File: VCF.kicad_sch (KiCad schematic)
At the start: 79 parts, among them K10 SW_SPST, K7 SW_SPST, K8 SW_SPST, K9 SW_SPST, P10 100k, P11 100k, P12 100k, P14 100k, P16 22k, P8 50k, P9 50k, Q20 BF244A, Q21 BC214, Q22 BC214, Q23 BF244A, Q24 BC214, Q25 BC214, Q26 BC182B, U10 UA747, U12 CA3080A, U13 CA3080A, U8 UA747, U9 CA3080A

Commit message: Fix PCB errors
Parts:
- added C_Sin1 (x20): Conn_01x01, Connector_PinHeader_2.54mm:PinHeader_1x01_P2.54mm_Vertical, symbol Connector_Generic:Conn_01x01
- C25: footprint Capacitor_THT:CP_Radial_D6.3mm_P2.50mm -> Capacitor_THT:CP_Radial_D8.0mm_P5.00mm
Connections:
- net CV: now also C_Sin1.1 (Pin_1)
- net ENVELOPE: now also C_Sin1.1 (Pin_1)
- net LFO_OUT: now also C_Sin1.1 (Pin_1)
- net at C19.1, K10.2 (B), R91.1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: now also C_Sin1.1 (Pin_1)
- net at P14.1, Q24.1 (B), R116.2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: now also C_Sin1.1 (Pin_1)
- net at C18.2, P11.2, R98.1: now also C_Sin1.1 (Pin_1)
- net at P8.2, R95.1: now also C_Sin1.1 (Pin_1)
- net at P9.2, R96.1: now also C_Sin1.1 (Pin_1)
- net at P10.2, R97.1: now also C_Sin1.1 (Pin_1)
- net at K7.1 (A), R94.1: now also C_Sin1.1 (Pin_1)
- net at C22.1, K8.2 (B), Q23.3 (S)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: now also C_Sin1.1 (Pin_1)
- net at K9.2 (B), P12.1, Q20.3 (S)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: now also C_Sin1.1 (Pin_1), C_Sin1.1 (Pin_1)
- net at P14.2, R114.2: now also C_Sin1.1 (Pin_1)
- net at P16.3, R136.1: now also C_Sin1.1 (Pin_1)
- net at P12.2, R104.1: now also C_Sin1.1 (Pin_1)
- net at P12.3, R106.2: now also C_Sin1.1 (Pin_1)
- net at K8.1 (A), R123.2: now also C_Sin1.1 (Pin_1)
- net at K10.1 (A), R121.2: now also C_Sin1.1 (Pin_1)
- net at K9.1 (A), R122.2: now also C_Sin1.1 (Pin_1)
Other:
- note removed: "15V? Or GND?"
- moved on the sheet: C22, K10, K7, K8, K9, P10, P11, P8, P9, R104, R106, R108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

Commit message: Kicad update
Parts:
- renumbered C_Sin1 to K10-1, C_Sin1 to K10-2, C_Sin1 to K7-1, C_Sin1 to K7-2, C_Sin1 to K8-1, C_Sin1 to K8-2, C_Sin1 to K9-1, C_Sin1 to K9-2, C_Sin1 to P10-3, C_Sin1 to P11-3, C_Sin1 to P12-1, C_Sin1 to P12-2, C_Sin1 to P12-3, C_Sin1 to P13-1, C_Sin1 to P14-1, C_Sin1 to P14-3, C_Sin1 to P8-1, C_Sin1 to P8-3, C_Sin1 to P9-1, C_Sin1 to P9-3

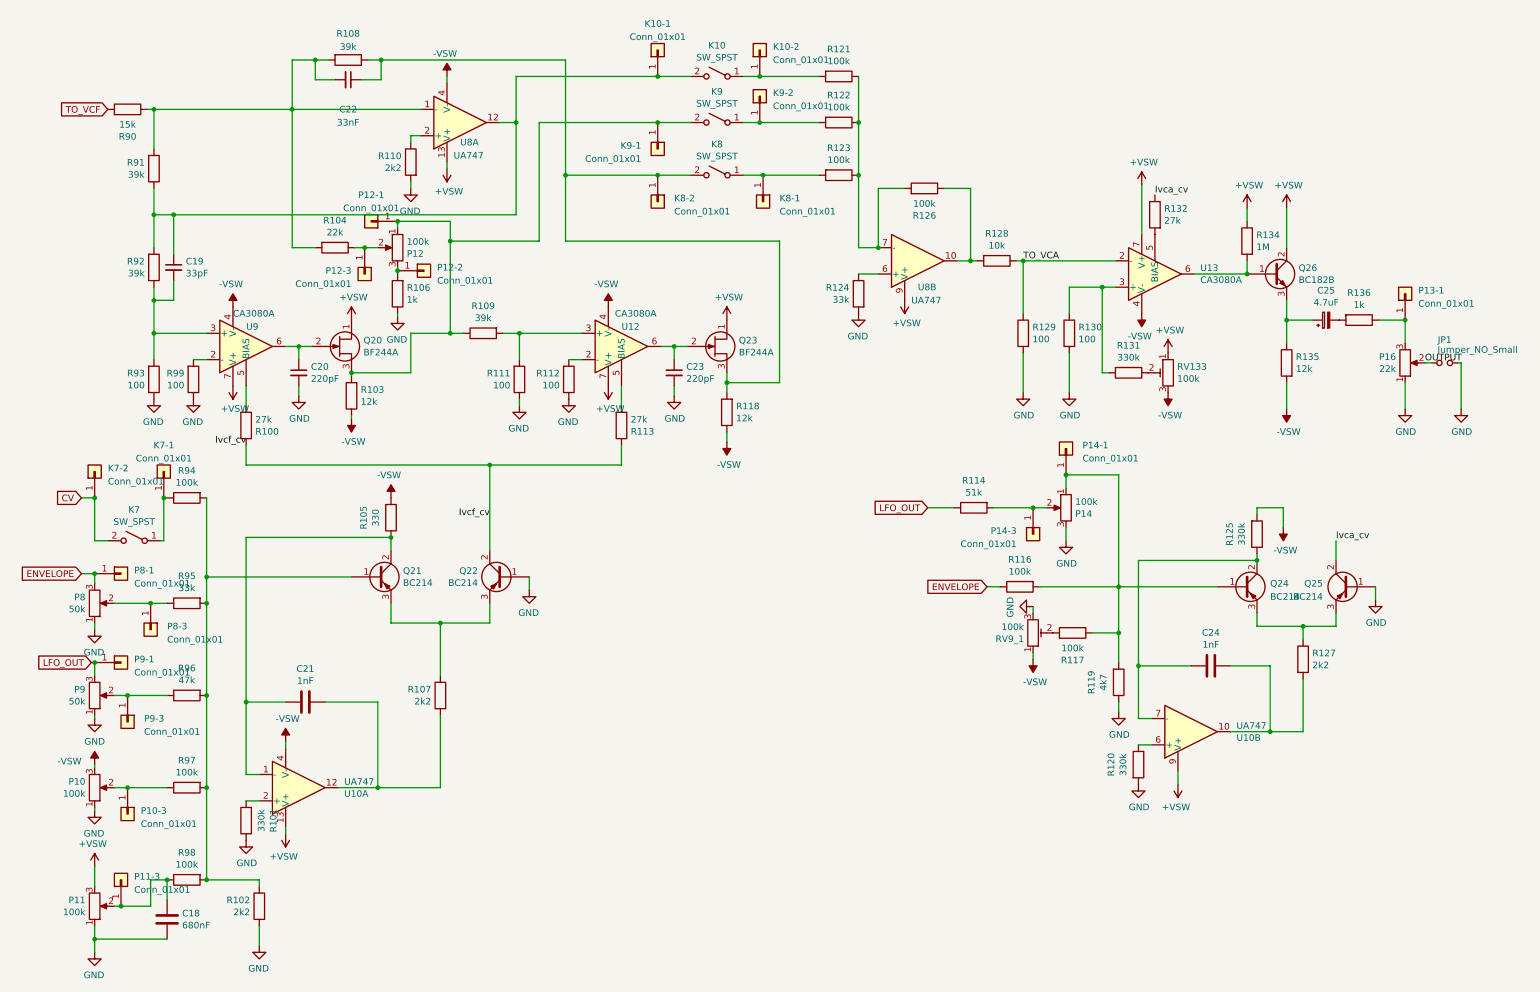
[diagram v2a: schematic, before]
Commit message: Replace symbols with new library
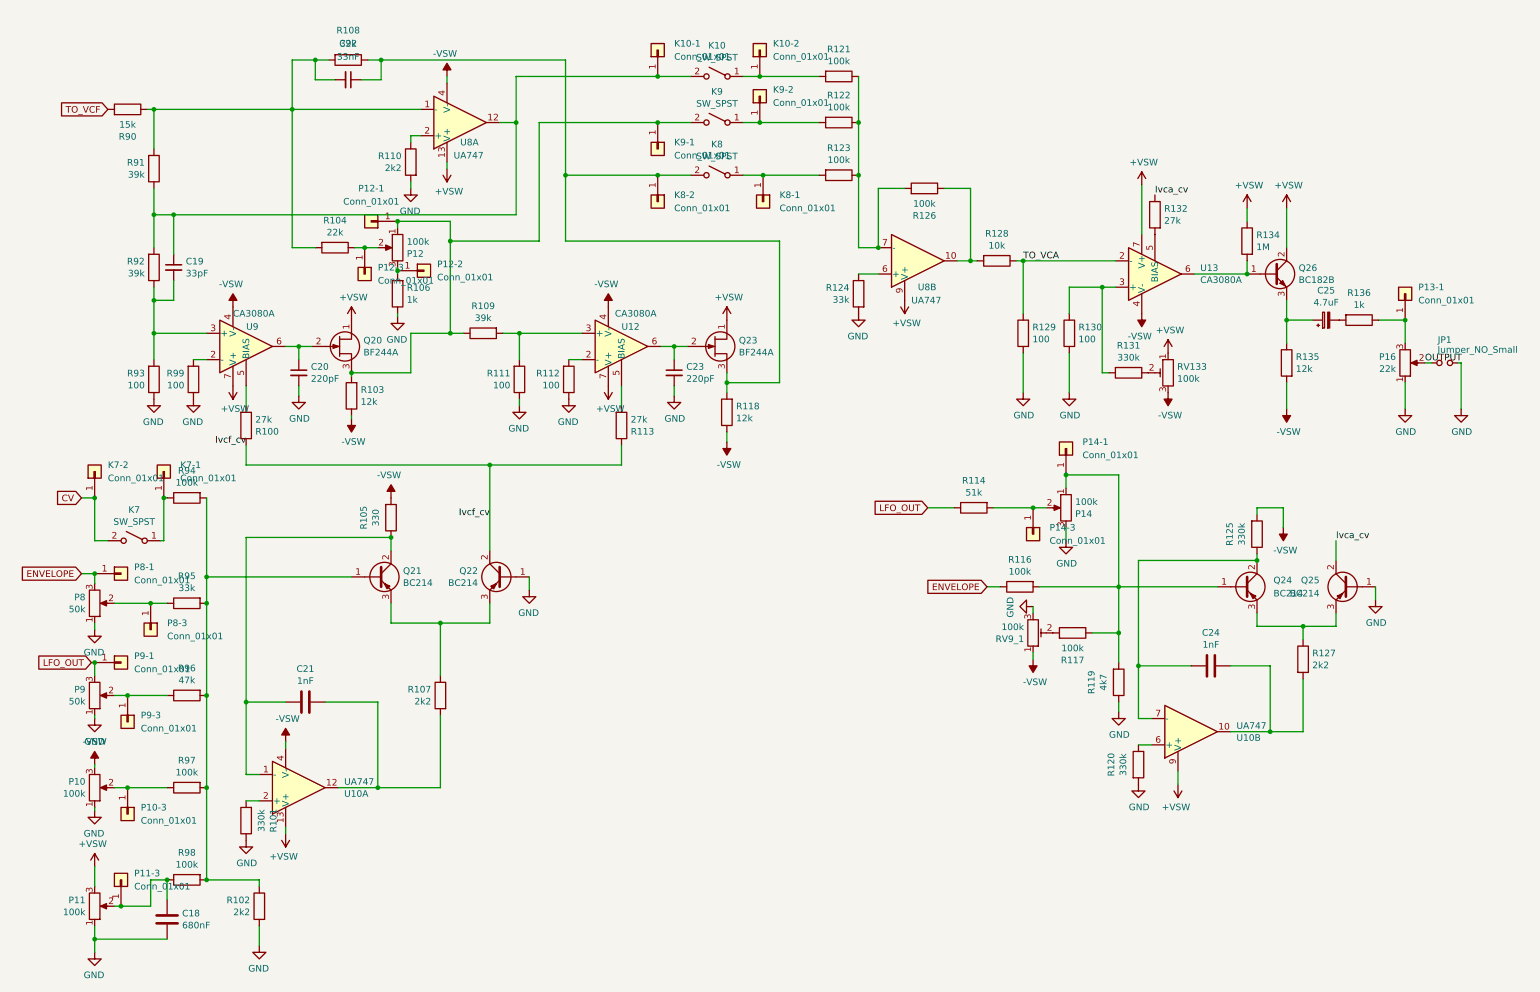
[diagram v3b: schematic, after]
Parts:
- C18, C19, C20, C21, C22, C23, C24: footprint Capacitor_THT:C_Disc_D5.0mm_W2.5mm_P5.00mm -> (none)
- C25: footprint Capacitor_THT:CP_Radial_D8.0mm_P5.00mm -> (none)
- JP1: footprint Connector_PinHeader_2.54mm:PinHeader_1x02_P2.54mm_Vertical -> (none)
- K10, K7, K8, K9, P10, P11, P12, P14, P16, P8, P9: footprint Connector_PinSocket_2.54mm:PinSocket_1x03_P2.54mm_Vertical -> (none)
- K10-1, K10-2, K7-1, K7-2, K8-1, K8-2, K9-1, K9-2, P10-3, P11-3, P12-1, P12-2, P12-3, P13-1, P14-1, P14-3, P8-1, P8-3, P9-1, P9-3: footprint Connector_PinHeader_2.54mm:PinHeader_1x01_P2.54mm_Vertical -> (none)
- Q20, Q23: footprint Package_TO_SOT_THT:TO-92L_Inline_Wide -> Package_TO_SOT_THT:TO-92_Inline
- Q21, Q22, Q24, Q25: symbol Device:Q_PNP_BCE -> Transistor_BJT:Q_PNP_BCE
- Q26: symbol Device:Q_NPN_BCE -> Transistor_BJT:Q_NPN_BCE
- R100, R101, R102, R103, R104, R105, R106, R107, R108, R109, R110, R111, R112, R113, R114, R116, R117, R118, R119, R120, R121, R122, R123, R124, R125, R126, R127, R128, R129, R130, R131, R132, R134, R135, R136, R90, R91, R92, R93, R94, R95, R96, R97, R98, R99: footprint Resistor_THT:R_Axial_DIN0207_L6.3mm_D2.5mm_P15.24mm_Horizontal -> (none)
- RV133, RV9_1: footprint Potentiometer_THT:Potentiometer_Bourns_3296W_Vertical -> (none)
- U10, U8: footprint Package_DIP:DIP-14_W7.62mm_Socket_LongPads -> (none)
- U12, U13, U9: footprint Package_DIP:DIP-8_W7.62mm_Socket_LongPads -> (none)

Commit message: Label connectors, update footprints
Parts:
- C18, C19, C20, C21, C22, C23, C24: footprint (none) -> Capacitor_THT:C_Disc_D5.0mm_W2.5mm_P5.00mm
- C25: footprint (none) -> Capacitor_THT:CP_Radial_D8.0mm_P5.00mm
- K10-1, K10-2, K7-1, K7-2, K8-1, K8-2, K9-1, K9-2, P10-3, P11-3, P12-1, P12-2, P12-3, P13-1, P14-1, P14-3, P8-1, P8-3, P9-1, P9-3: footprint (none) -> Connector_PinHeader_2.54mm:PinHeader_1x01_P2.54mm_Vertical
- Q23: footprint Package_TO_SOT_THT:TO-92_Inline -> Package_TO_SOT_THT:TO-92_Inline_Wide
- R100, R101, R102, R103, R104, R105, R106, R107, R108, R109, R110, R111, R112, R113, R114, R116, R117, R118, R119, R120, R121, R122, R123, R124, R125, R126, R127, R128, R129, R130, R131, R132, R134, R135, R136, R90, R91, R92, R93, R94, R95, R96, R97, R98, R99: footprint (none) -> Resistor_THT:R_Axial_DIN0207_L6.3mm_D2.5mm_P15.24mm_Horizontal
- RV133, RV9_1: footprint (none) -> Potentiometer_THT:Potentiometer_Bourns_3296W_Vertical
- U10, U8: footprint (none) -> Package_DIP:DIP-14_W7.62mm_Socket_LongPads
- U12, U13, U9: footprint (none) -> Package_DIP:DIP-8_W7.62mm_Socket_LongPads
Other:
- note added: "BP"
- note added: "CUTOFF"
- note added: "HP"
- note added: "LP"
- note added: "RESONANCE"
- note added: "VCF MIN"
- moved on the sheet: K10, K10-1, K10-2, K8, K8-1, K8-2, K9, K9-1, K9-2, P11-3, R121, R122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
